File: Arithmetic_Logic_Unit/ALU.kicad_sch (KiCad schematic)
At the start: 32 parts, among them U10 74LS245, U11 74LS173, U4 74LS08, U5 74LS86, U6 74LS86, U7 74LS02, U8 74LS283, U9 74LS283

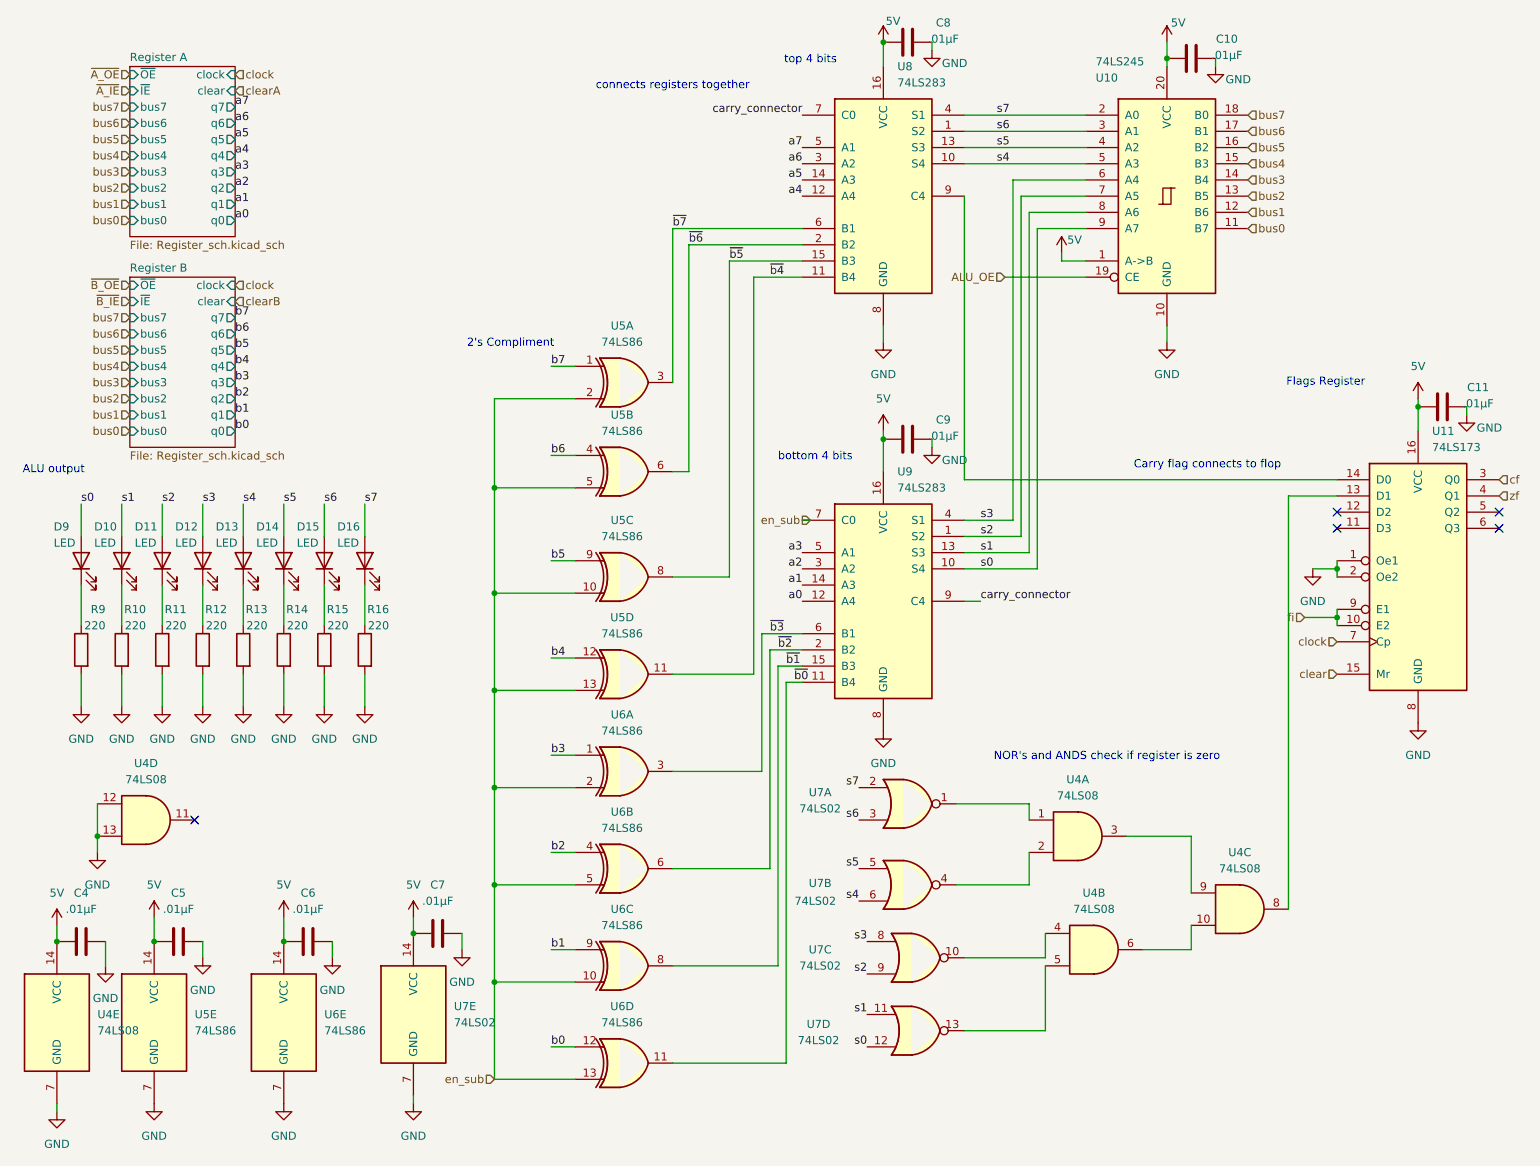
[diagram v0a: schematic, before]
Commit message: updated Arithemetic Logic Unit
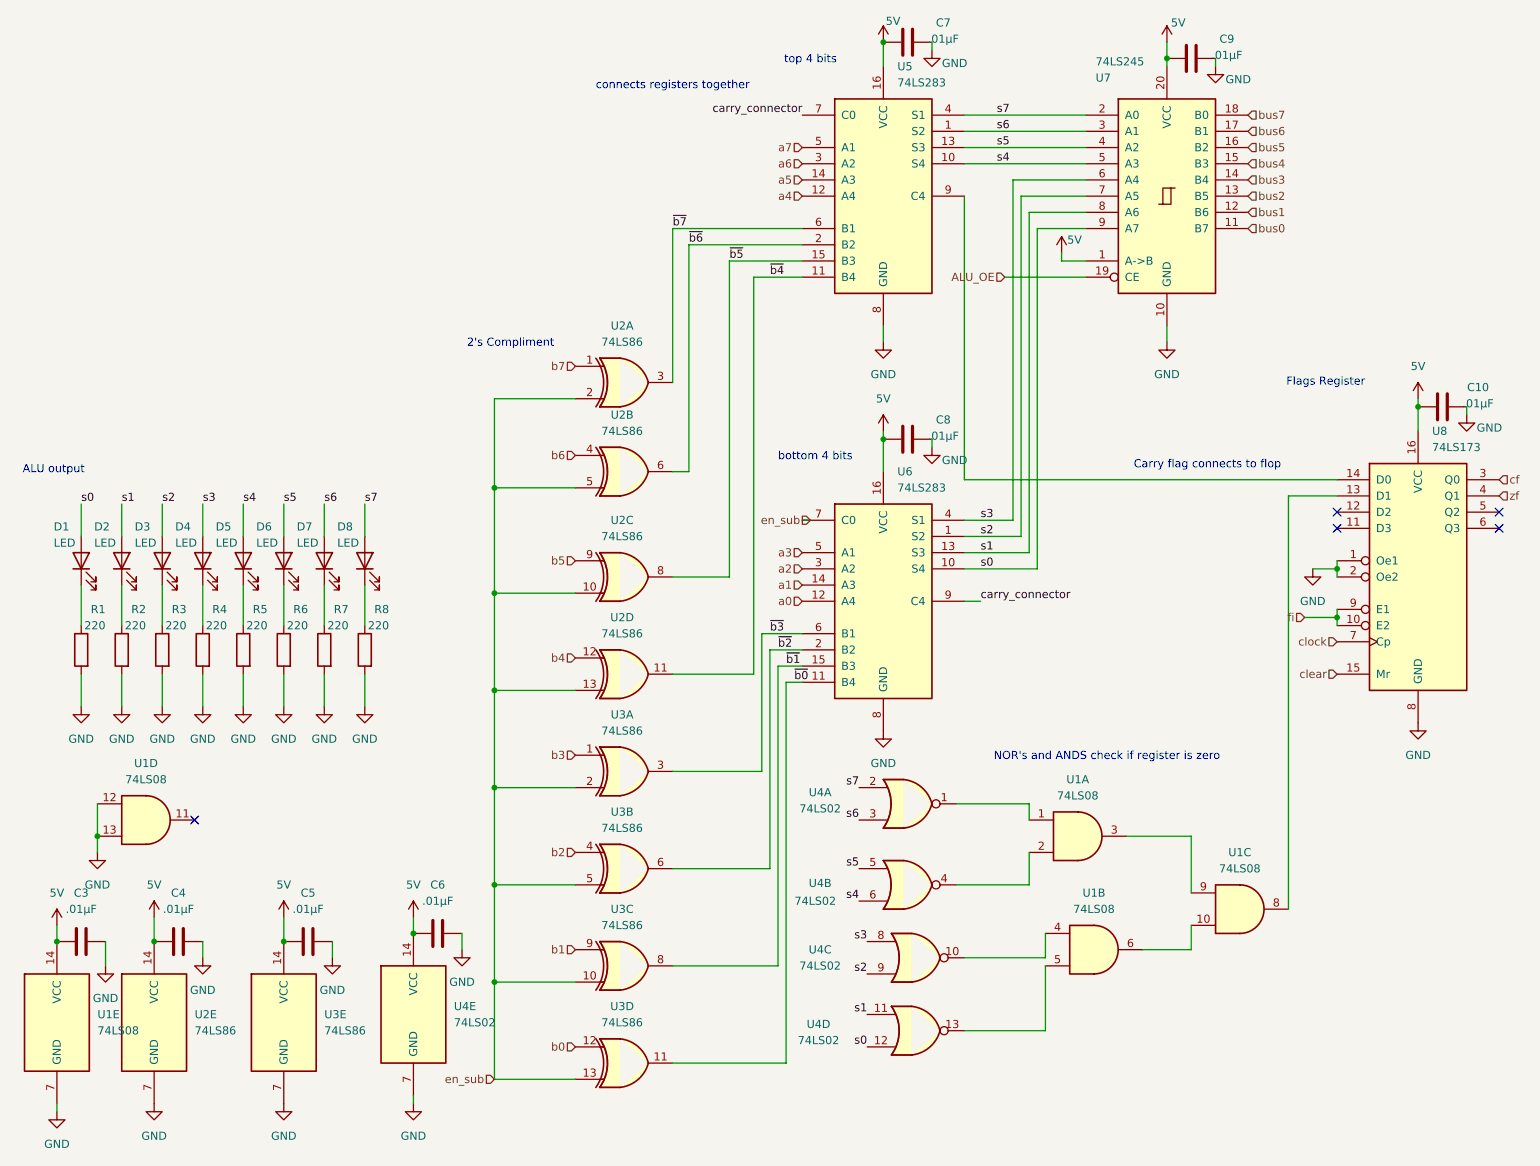
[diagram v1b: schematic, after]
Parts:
- renumbered C11 to C10, C4 to C3, C5 to C4, C6 to C5, C7 to C6, C8 to C7, C9 to C8, C10 to C9, D9 to D1, D10 to D2, D11 to D3, D12 to D4, D13 to D5, D14 to D6, D15 to D7, D16 to D8, R9 to R1, R10 to R2, R11 to R3, R12 to R4, R13 to R5, R14 to R6, R15 to R7, R16 to R8, U4 to U1, U5 to U2, U6 to U3, U7 to U4, U8 to U5, U9 to U6, U10 to U7, U11 to U8
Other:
- removed sheet Register A
- removed sheet Register B

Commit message: fixed Ram register, fixed mar in ram.v, updated caps in alu, ram, and instruction register
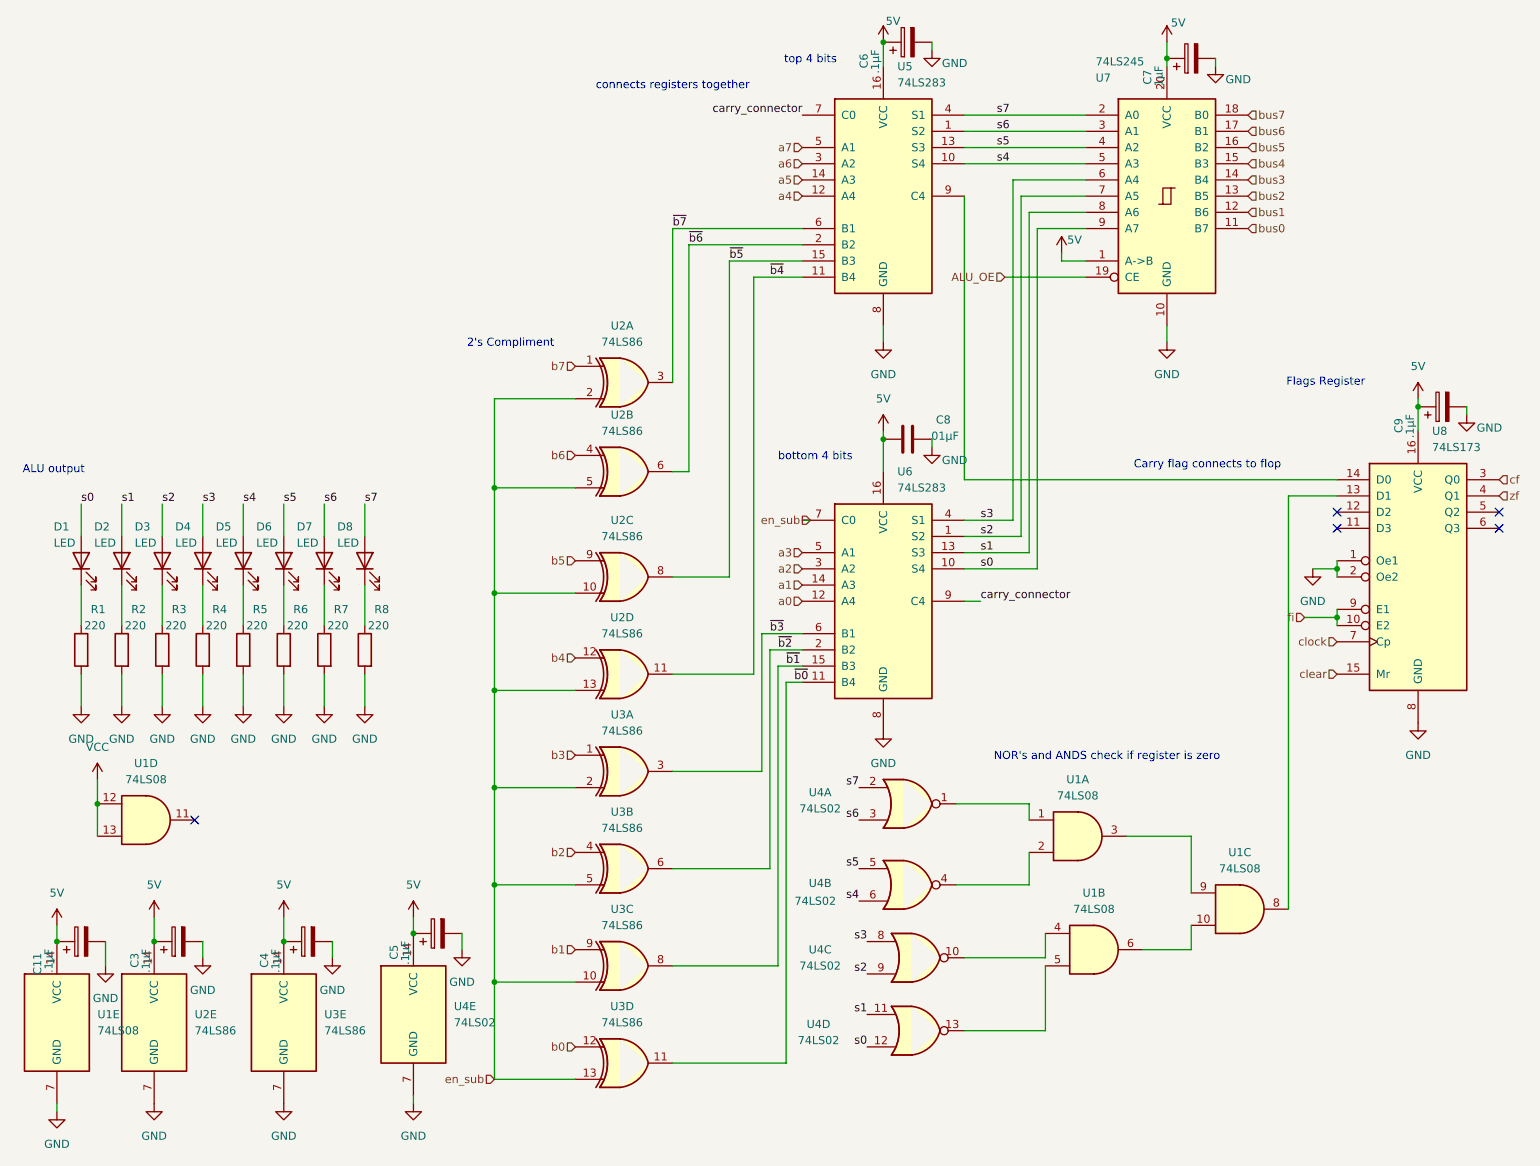
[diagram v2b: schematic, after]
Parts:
- removed C10, C3, C4, C5, C6, C7, C9: .01µF, Capacitor_THT:C_Disc_D5.0mm_W2.5mm_P2.50mm, symbol Device:C
- added C11, C3, C4, C5, C6, C7, C9: .1µF, symbol Device:C_Polarized
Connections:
- net 5V: now also C11.1, C3.1, C4.1, C5.1, C6.1, C7.1, C9.1
- net GND: now also C11.2, C3.2, C4.2, C5.2, C6.2, C7.2, C9.2; no longer U1.12, U1.13
- new net VCC: U1.12, U1.13
